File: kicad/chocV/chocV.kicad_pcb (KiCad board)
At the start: 2 copper layers, 212.5 x 78.7 mm, 84 parts, among them SW1 SW_Push, SW10 SW_Push, SW11 SW_Push, SW12 SW_Push, SW13 SW_Push, SW14 SW_Push, SW15 SW_Push, SW16 SW_Push, SW17 SW_Push, SW18 SW_Push, SW19 SW_Push, SW2 SW_Push, SW20 SW_Push, SW21 SW_Push, SW22 SW_Push, SW23 SW_Push, SW24 SW_Push, SW25 SW_Push, SW26 SW_Push, SW27 SW_Push, SW28 SW_Push, SW29 SW_Push, SW3 SW_Push, SW30 SW_Push, SW31 SW_Push, SW32 SW_Push, SW33 SW_Push, SW34 SW_Push, SW35 SW_Push, SW36 SW_Push, SW37 Reset Switch, SW38 Switch_SW_DIP_x01, SW4 SW_Push, SW5 SW_Push, SW6 SW_Push, SW7 SW_Push, SW8 SW_Push, SW9 SW_Push, U1 Pro-Micro

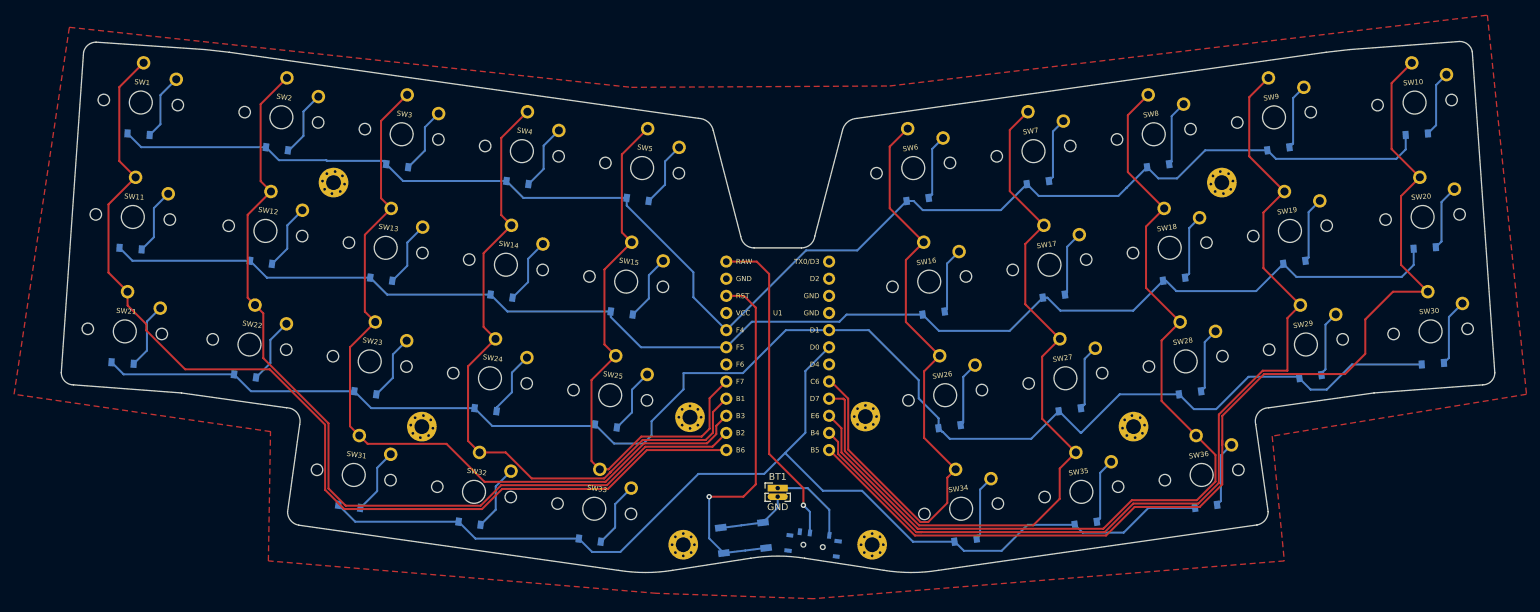
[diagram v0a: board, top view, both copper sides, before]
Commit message: Update PCB and Schematic
Add battery_pads
Switch PCB bottom side to ground plane
Move reset and power cut-off switches close to the border
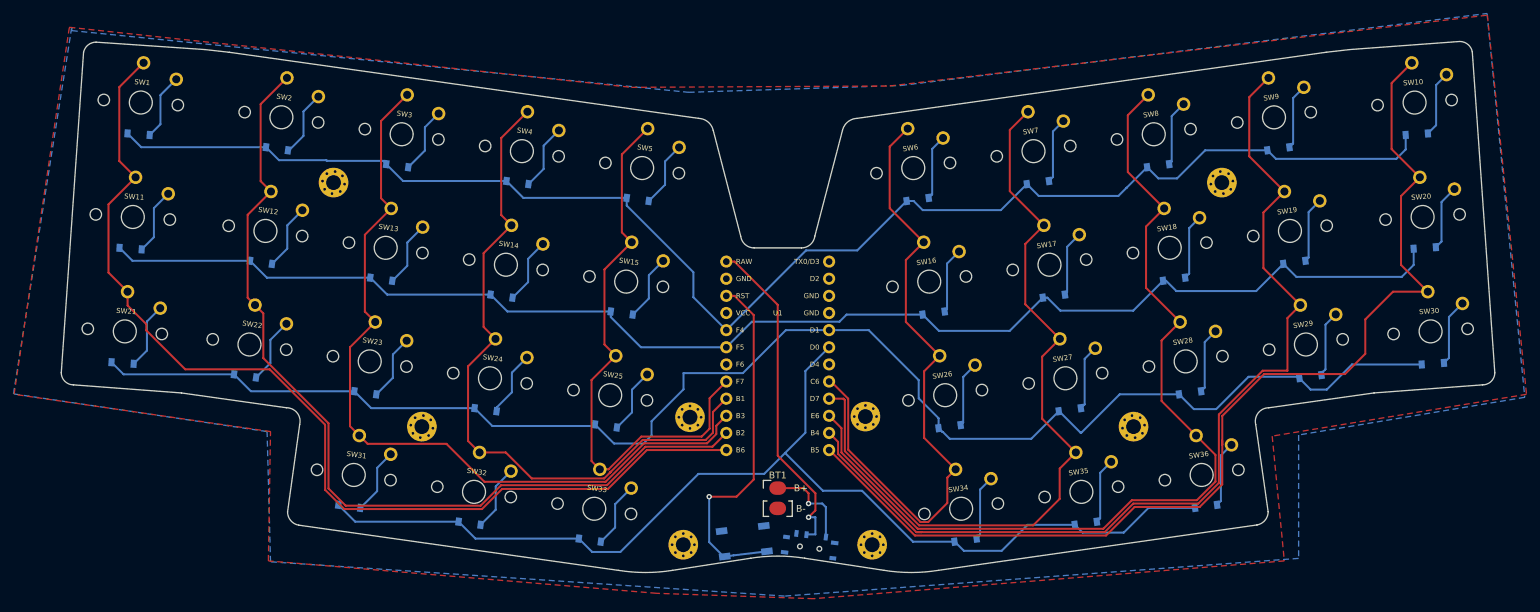
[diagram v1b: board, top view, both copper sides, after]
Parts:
- BT1: value Device_Battery_Cell -> Battery_Cell; footprint other:PinHeader_1x02_P1.27mm_Vertical -> other:battery_pads
- moved SW38 0.57 mm to (114.6, 94.8)
- moved SW37 0.52 mm to (105.0, 92.5)
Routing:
- net ground: track 10.9 -> 0.19 mm
- net raw: track 48.0 -> 49.7 mm
- net Net-(BT1-Pad1): track 12.4 -> 13.6 mm, vias 0 -> 1
- net reset: track 54.7 -> 53.7 mm
- added copper zone on B.Cu, net ground
